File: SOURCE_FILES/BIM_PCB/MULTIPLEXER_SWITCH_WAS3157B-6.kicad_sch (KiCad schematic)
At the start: 4 parts, among them U14 WAS3157B, U15 WAS3157B

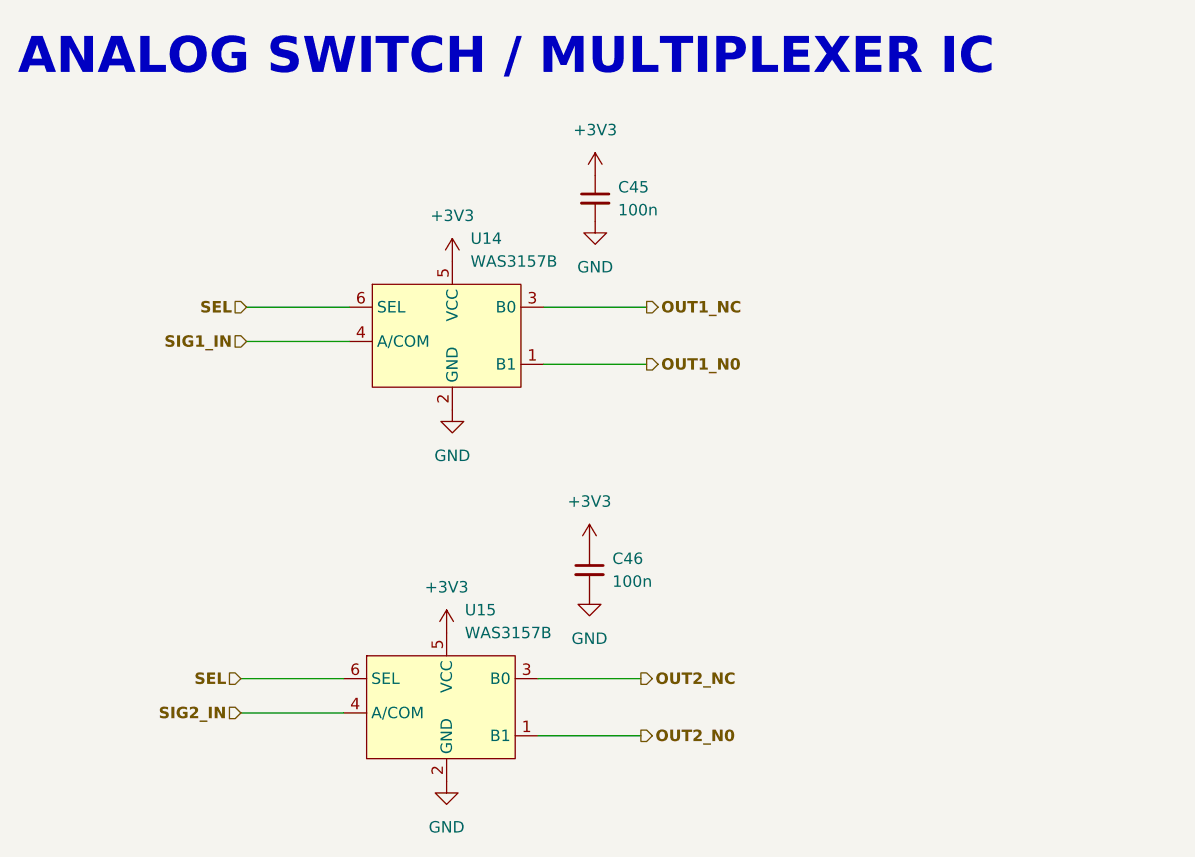
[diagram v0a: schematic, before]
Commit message: updates on the buck 3v3 supply
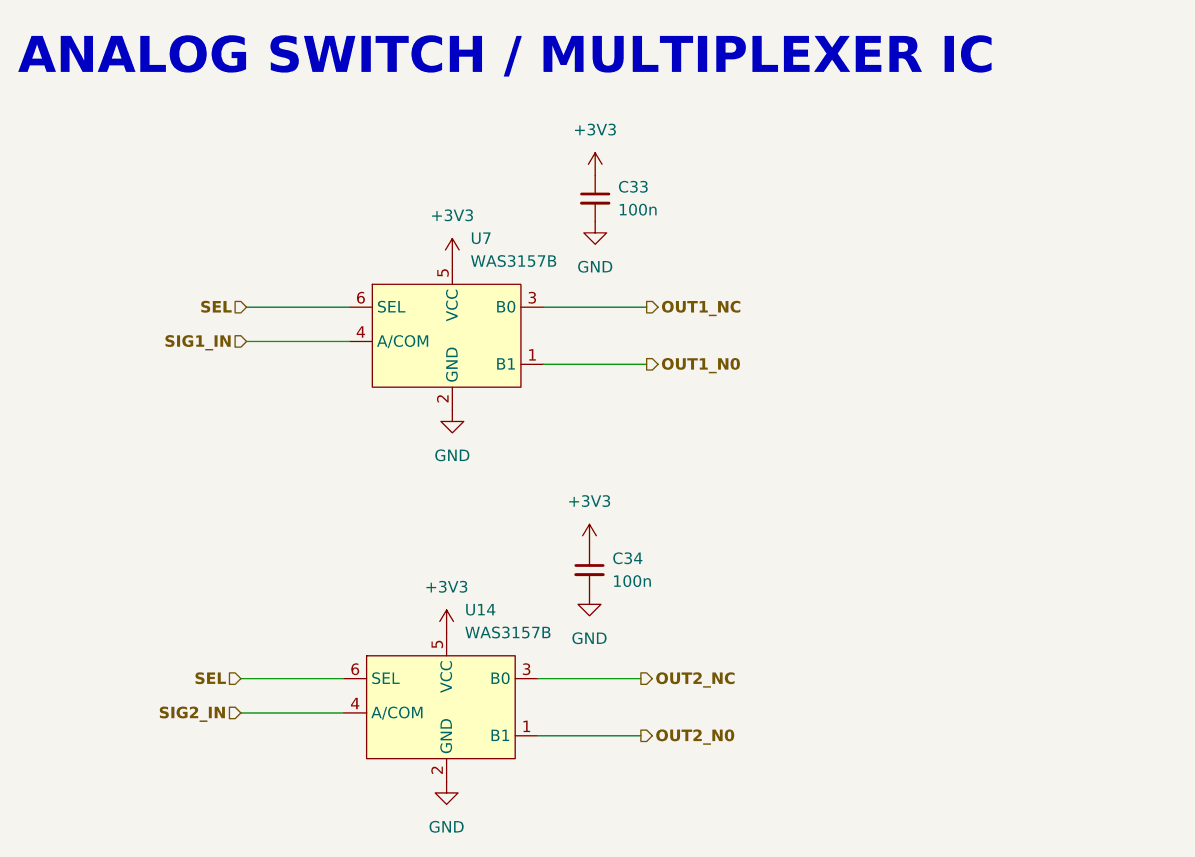
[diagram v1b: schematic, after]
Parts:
- C33: renamed from C45; footprint Capacitor_SMD:C_0603_1608Metric -> Capacitor_SMD:C_0402_1005Metric
- C34: renamed from C46; footprint Capacitor_SMD:C_0603_1608Metric -> Capacitor_SMD:C_0402_1005Metric
- renumbered U15 to U14, U14 to U7
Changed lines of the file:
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@@
   (symbol (lib_id "power:GND") (at 139.065 125.095 0) (unit 1)
     (in_bom yes) (on_board yes) (dnp no) (fields_autoplaced)
-    (property "Reference" "#PWR0101" (at 139.065 131.445 0)
+    (property "Reference" "#PWR069" (at 139.065 131.445 0)
       (effects (font (size 1.27 1.27)) hide)
     )
@@
     (instances
       (project "BIM_PCB"
-        (path "/b79ebed7-e146-448b-8dab-0aefb3e182ca/e46c25ff-852f-4c6f-87a8-4f698594cba1"
-          (reference "#PWR0101") (unit 1)
-        )
-        (path "/b79ebed7-e146-448b-8dab-0aefb3e182ca/047083e0-3635-4a91-810f-870f48791e28"
-          (reference "#PWR0109") (unit 1)
+        (path "/b79ebed7-e146-448b-8dab-0aefb3e182ca/5db0ebc2-0f98-4304-ae29-c0117022d2f4"
+          (reference "#PWR069") (unit 1)
         )
       )
@@
   (symbol (lib_id "GCL_Integrated-Circuits:WAS3157B") (at 127.635 111.125 0) (unit 1)
     (in_bom yes) (on_board yes) (dnp no) (fields_autoplaced)
-    (property "Reference" "U15" (at 141.0844 106.045 0)
+    (property "Reference" "U14" (at 141.0844 106.045 0)
       (effects (font (size 1.27 1.27)) (justify left))
     )
@@
     (instances
       (project "BIM_PCB"
-        (path "/b79ebed7-e146-448b-8dab-0aefb3e182ca/e46c25ff-852f-4c6f-87a8-4f698594cba1"
-          (reference "U15") (unit 1)
-        )
-        (path "/b79ebed7-e146-448b-8dab-0aefb3e182ca/047083e0-3635-4a91-810f-870f48791e28"
-          (reference "U17") (unit 1)
+        (path "/b79ebed7-e146-448b-8dab-0aefb3e182ca/5db0ebc2-0f98-4304-ae29-c0117022d2f4"
+          (reference "U14") (unit 1)
         )
       )
@@
   (symbol (lib_id "power:+3V3") (at 155.575 57.785 0) (unit 1)
     (in_bom yes) (on_board yes) (dnp no) (fields_autoplaced)
-    (property "Reference" "#PWR020" (at 155.575 61.595 0)
+    (property "Reference" "#PWR062" (at 155.575 61.595 0)
       (effects (font (size 1.27 1.27)) hide)
     )
@@
     (instances
       (project "BIM_PCB"
-        (path "/b79ebed7-e146-448b-8dab-0aefb3e182ca/e46c25ff-852f-4c6f-87a8-4f698594cba1"
-          (reference "#PWR020") (unit 1)
-        )
-        (path "/b79ebed7-e146-448b-8dab-0aefb3e182ca/047083e0-3635-4a91-810f-870f48791e28"
-          (reference "#PWR0102") (unit 1)
+        (path "/b79ebed7-e146-448b-8dab-0aefb3e182ca/5db0ebc2-0f98-4304-ae29-c0117022d2f4"
+          (reference "#PWR062") (unit 1)
         )
       )
@@
   (symbol (lib_id "Device:C_Small") (at 155.575 60.325 0) (unit 1)
     (in_bom yes) (on_board yes) (dnp no) (fields_autoplaced)
-    (property "Reference" "C45" (at 158.115 59.0612 0)
+    (property "Reference" "C33" (at 158.115 59.0612 0)
       (effects (font (size 1.27 1.27)) (justify left))
     )
@@
       (effects (font (size 1.27 1.27)) (justify left))
     )
-    (property "Footprint" "Capacitor_SMD:C_0603_1608Metric" (at 155.575 60.325 0)
+    (property "Footprint" "Capacitor_SMD:C_0402_1005Metric" (at 155.575 60.325 0)
       (effects (font (size 1.27 1.27)) hide)
     )
@@
     (instances
       (project "BIM_PCB"
-        (path "/b79ebed7-e146-448b-8dab-0aefb3e182ca/e46c25ff-852f-4c6f-87a8-4f698594cba1"
-          (reference "C45") (unit 1)
-        )
-        (path "/b79ebed7-e146-448b-8dab-0aefb3e182ca/047083e0-3635-4a91-810f-870f48791e28"
-          (reference "C47") (unit 1)
+        (path "/b79ebed7-e146-448b-8dab-0aefb3e182ca/5db0ebc2-0f98-4304-ae29-c0117022d2f4"
+          (reference "C33") (unit 1)
         )
       )
@@
   (symbol (lib_id "power:+3V3") (at 139.7 67.31 0) (unit 1)
     (in_bom yes) (on_board yes) (dnp no) (fields_autoplaced)
-    (property "Reference" "#PWR096" (at 139.7 71.12 0)
+    (property "Reference" "#PWR064" (at 139.7 71.12 0)
       (effects (font (size 1.27 1.27)) hide)
     )
@@
     (instances
       (project "BIM_PCB"
-        (path "/b79ebed7-e146-448b-8dab-0aefb3e182ca/e46c25ff-852f-4c6f-87a8-4f698594cba1"
-          (reference "#PWR096") (unit 1)
-        )
-        (path "/b79ebed7-e146-448b-8dab-0aefb3e182ca/047083e0-3635-4a91-810f-870f48791e28"
-          (reference "#PWR0104") (unit 1)
+        (path "/b79ebed7-e146-448b-8dab-0aefb3e182ca/5db0ebc2-0f98-4304-ae29-c0117022d2f4"
+          (reference "#PWR064") (unit 1)
         )
       )
@@
   (symbol (lib_id "power:+3V3") (at 139.065 108.585 0) (unit 1)
     (in_bom yes) (on_board yes) (dnp no) (fields_autoplaced)
-    (property "Reference" "#PWR0100" (at 139.065 112.395 0)
+    (property "Reference" "#PWR068" (at 139.065 112.395 0)
       (effects (font (size 1.27 1.27)) hide)
     )
@@
     (instances
       (project "BIM_PCB"
-        (path "/b79ebed7-e146-448b-8dab-0aefb3e182ca/e46c25ff-852f-4c6f-87a8-4f698594cba1"
-          (reference "#PWR0100") (unit 1)
-        )
-        (path "/b79ebed7-e146-448b-8dab-0aefb3e182ca/047083e0-3635-4a91-810f-870f48791e28"
-          (reference "#PWR0108") (unit 1)
+        (path "/b79ebed7-e146-448b-8dab-0aefb3e182ca/5db0ebc2-0f98-4304-ae29-c0117022d2f4"
+          (reference "#PWR068") (unit 1)
         )
       )
@@
   (symbol (lib_id "power:GND") (at 139.7 83.82 0) (unit 1)
     (in_bom yes) (on_board yes) (dnp no) (fields_autoplaced)
-    (property "Reference" "#PWR097" (at 139.7 90.17 0)
+    (property "Reference" "#PWR065" (at 139.7 90.17 0)
       (effects (font (size 1.27 1.27)) hide)
     )
@@
     (instances
       (project "BIM_PCB"
-        (path "/b79ebed7-e146-448b-8dab-0aefb3e182ca/e46c25ff-852f-4c6f-87a8-4f698594cba1"
-          (reference "#PWR097") (unit 1)
-        )
-        (path "/b79ebed7-e146-448b-8dab-0aefb3e182ca/047083e0-3635-4a91-810f-870f48791e28"
-          (reference "#PWR0105") (unit 1)
+        (path "/b79ebed7-e146-448b-8dab-0aefb3e182ca/5db0ebc2-0f98-4304-ae29-c0117022d2f4"
+          (reference "#PWR065") (unit 1)
         )
       )
@@
   (symbol (lib_id "Device:C_Small") (at 154.94 101.6 0) (unit 1)
     (in_bom yes) (on_board yes) (dnp no) (fields_autoplaced)
-    (property "Reference" "C46" (at 157.48 100.3362 0)
+    (property "Reference" "C34" (at 157.48 100.3362 0)
       (effects (font (size 1.27 1.27)) (justify left))
     )
@@
       (effects (font (size 1.27 1.27)) (justify left))
     )
-    (property "Footprint" "Capacitor_SMD:C_0603_1608Metric" (at 154.94 101.6 0)
+    (property "Footprint" "Capacitor_SMD:C_0402_1005Metric" (at 154.94 101.6 0)
       (effects (font (size 1.27 1.27)) hide)
     )
@@
     (instances
       (project "BIM_PCB"
-        (path "/b79ebed7-e146-448b-8dab-0aefb3e182ca/e46c25ff-852f-4c6f-87a8-4f698594cba1"
-          (reference "C46") (unit 1)
-        )
-        (path "/b79ebed7-e146-448b-8dab-0aefb3e182ca/047083e0-3635-4a91-810f-870f48791e28"
-          (reference "C48") (unit 1)
+        (path "/b79ebed7-e146-448b-8dab-0aefb3e182ca/5db0ebc2-0f98-4304-ae29-c0117022d2f4"
+          (reference "C34") (unit 1)
         )
       )
@@
   (symbol (lib_id "GCL_Integrated-Circuits:WAS3157B") (at 128.27 69.85 0) (unit 1)
     (in_bom yes) (on_board yes) (dnp no) (fields_autoplaced)
-    (property "Reference" "U14" (at 141.7194 64.77 0)
+    (property "Reference" "U7" (at 141.7194 64.77 0)
       (effects (font (size 1.27 1.27)) (justify left))
     )
@@
     (instances
       (project "BIM_PCB"
-        (path "/b79ebed7-e146-448b-8dab-0aefb3e182ca/e46c25ff-852f-4c6f-87a8-4f698594cba1"
-          (reference "U14") (unit 1)
-        )
-        (path "/b79ebed7-e146-448b-8dab-0aefb3e182ca/047083e0-3635-4a91-810f-870f48791e28"
-          (reference "U16") (unit 1)
+        (path "/b79ebed7-e146-448b-8dab-0aefb3e182ca/5db0ebc2-0f98-4304-ae29-c0117022d2f4"
+          (reference "U7") (unit 1)
         )
       )
@@
   (symbol (lib_id "power:GND") (at 155.575 62.865 0) (unit 1)
     (in_bom yes) (on_board yes) (dnp no) (fields_autoplaced)
-    (property "Reference" "#PWR021" (at 155.575 69.215 0)
+    (property "Reference" "#PWR063" (at 155.575 69.215 0)
       (effects (font (size 1.27 1.27)) hide)
     )
@@
     (instances
       (project "BIM_PCB"
-        (path "/b79ebed7-e146-448b-8dab-0aefb3e182ca/e46c25ff-852f-4c6f-87a8-4f698594cba1"
-          (reference "#PWR021") (unit 1)
-        )
-        (path "/b79ebed7-e146-448b-8dab-0aefb3e182ca/047083e0-3635-4a91-810f-870f48791e28"
-          (reference "#PWR0103") (unit 1)
+        (path "/b79ebed7-e146-448b-8dab-0aefb3e182ca/5db0ebc2-0f98-4304-ae29-c0117022d2f4"
+          (reference "#PWR063") (unit 1)
         )
       )
@@
   (symbol (lib_id "power:+3V3") (at 154.94 99.06 0) (unit 1)
     (in_bom yes) (on_board yes) (dnp no) (fields_autoplaced)
-    (property "Reference" "#PWR098" (at 154.94 102.87 0)
+    (property "Reference" "#PWR066" (at 154.94 102.87 0)
       (effects (font (size 1.27 1.27)) hide)
     )
@@
     (instances
       (project "BIM_PCB"
-        (path "/b79ebed7-e146-448b-8dab-0aefb3e182ca/e46c25ff-852f-4c6f-87a8-4f698594cba1"
-          (reference "#PWR098") (unit 1)
-        )
-        (path "/b79ebed7-e146-448b-8dab-0aefb3e182ca/047083e0-3635-4a91-810f-870f48791e28"
-          (reference "#PWR0106") (unit 1)
+        (path "/b79ebed7-e146-448b-8dab-0aefb3e182ca/5db0ebc2-0f98-4304-ae29-c0117022d2f4"
+          (reference "#PWR066") (unit 1)
         )
       )
@@
   (symbol (lib_id "power:GND") (at 154.94 104.14 0) (unit 1)
     (in_bom yes) (on_board yes) (dnp no) (fields_autoplaced)
-    (property "Reference" "#PWR099" (at 154.94 110.49 0)
+    (property "Reference" "#PWR067" (at 154.94 110.49 0)
       (effects (font (size 1.27 1.27)) hide)
     )
@@
     (instances
       (project "BIM_PCB"
-        (path "/b79ebed7-e146-448b-8dab-0aefb3e182ca/e46c25ff-852f-4c6f-87a8-4f698594cba1"
-          (reference "#PWR099") (unit 1)
-        )
-        (path "/b79ebed7-e146-448b-8dab-0aefb3e182ca/047083e0-3635-4a91-810f-870f48791e28"
-          (reference "#PWR0107") (unit 1)
-        )
-      )
+        (path "/b79ebed7-e146-448b-8dab-0aefb3e182ca/5db0ebc2-0f98-4304-ae29-c0117022d2f4"
+          (reference "#PWR067") (unit 1)
+        )
+      )

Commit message: all items updated
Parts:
- U14, U7: value WAS3157B -> SN74LVC1G3157DBVR
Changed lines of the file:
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@@
   )
   (symbol (lib_id "GCL_Integrated-Circuits:WAS3157B") (at 127.635 111.125 0) (unit 1)
-    (in_bom yes) (on_board yes) (dnp no) (fields_autoplaced)
-    (property "Reference" "U14" (at 141.0844 106.045 0)
-      (effects (font (size 1.27 1.27)) (justify left))
-    )
-    (property "Value" "WAS3157B" (at 141.0844 108.585 0)
+    (in_bom yes) (on_board yes) (dnp no)
+    (property "Reference" "U14" (at 141.2591 106.68 0)
+      (effects (font (size 1.27 1.27)) (justify left))
+    )
+    (property "Value" "SN74LVC1G3157DBVR" (at 113.03 108.585 0)
       (effects (font (size 1.27 1.27)) (justify left))
     )
@@
   )
   (symbol (lib_id "GCL_Integrated-Circuits:WAS3157B") (at 128.27 69.85 0) (unit 1)
-    (in_bom yes) (on_board yes) (dnp no) (fields_autoplaced)
-    (property "Reference" "U7" (at 141.7194 64.77 0)
-      (effects (font (size 1.27 1.27)) (justify left))
-    )
-    (property "Value" "WAS3157B" (at 141.7194 67.31 0)
-      (effects (font (size 1.27 1.27)) (justify left))
-    )
+    (in_bom yes) (on_board yes) (dnp no)
+    (property "Reference" "U7" (at 141.8941 64.77 0)
+      (effects (font (size 1.27 1.27)) (justify left))
+    )
+    (property "Value" "SN74LVC1G3157DBVR" (at 115.57 67.945 0)
+      (effects (font (size 1.27 1.27)) (justify left))
+    )
